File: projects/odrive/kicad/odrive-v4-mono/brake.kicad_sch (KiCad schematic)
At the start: 29 parts, among them J13 BRAKE_EXT, Q50 NVMFS5C628NL/BSC027N10NS5, Q51 NVMFS5C628NL/BSC027N10NS5, U50 UCC27517A, U51 INA181A2, U52 TLV7031, U53 74LVC1G74, U54 74LVC1G32, U55 74LVC1G08

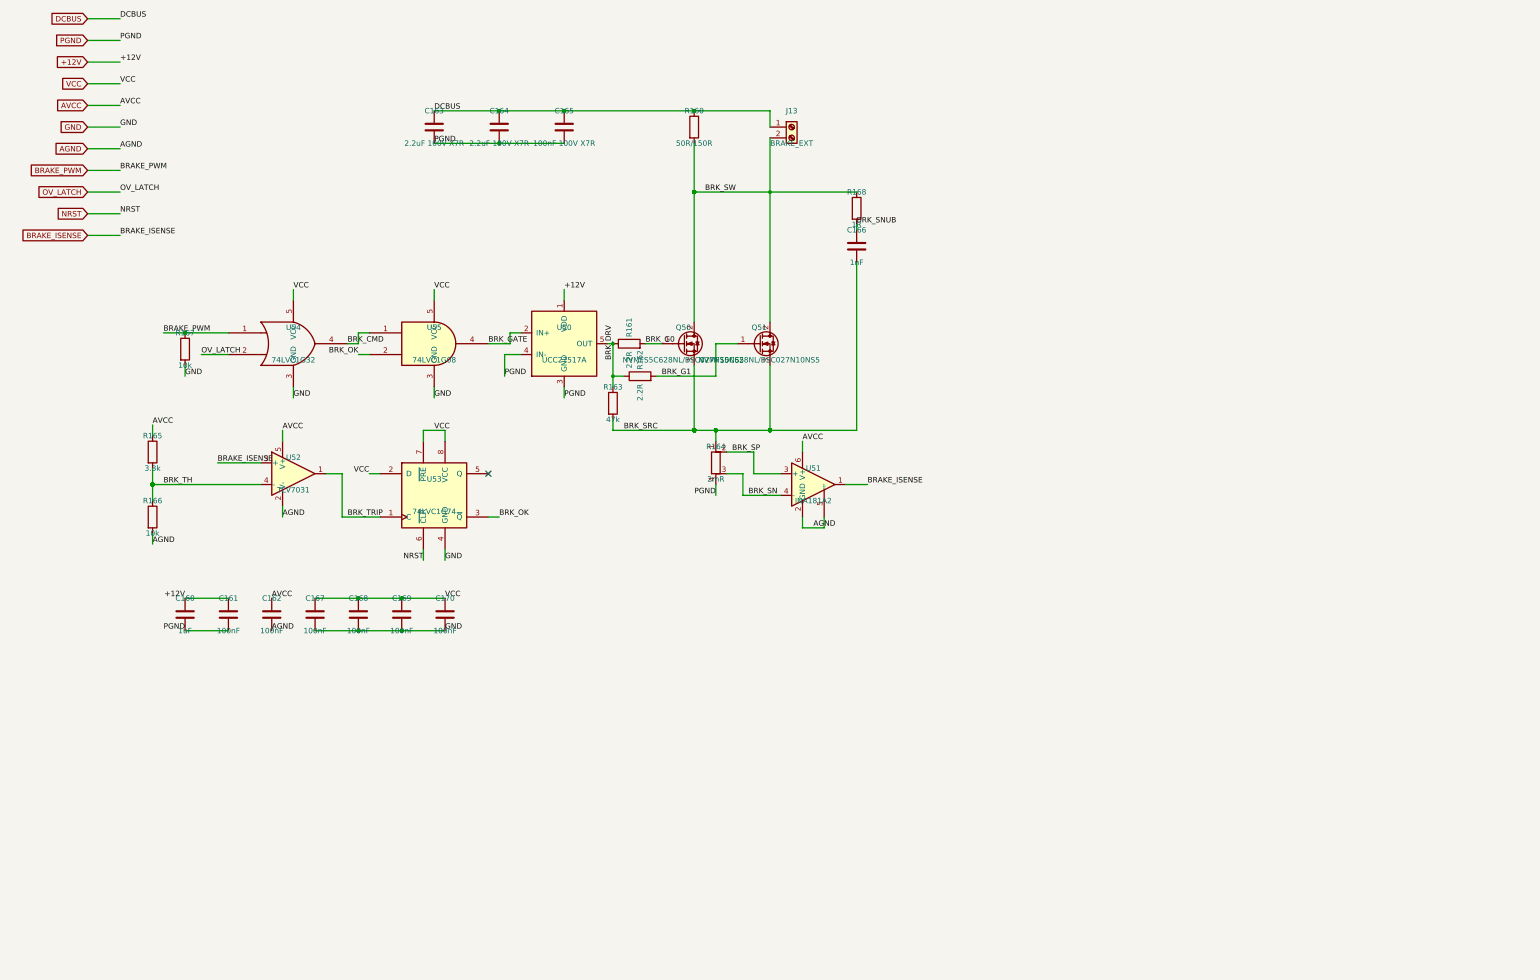
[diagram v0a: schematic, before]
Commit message: Checkpoint ODrive 56 V recovery and modular handoff
Preserve corrected schematics, local libraries, partial PCB routing, firmware diagnostics, analysis tools and the independent modular-study handoff. The board remains incomplete with 381 unconnected items and 415 DRC warnings.

Validation: 52 host tests, ARM component compilation, schematic/PCB parity, native copper preservation, DRC, STEP export, Python lint, shellcheck and nix fmt. Known Konnect-generated schematic whitespace is retained. No fabrication or hardware validation is claimed.
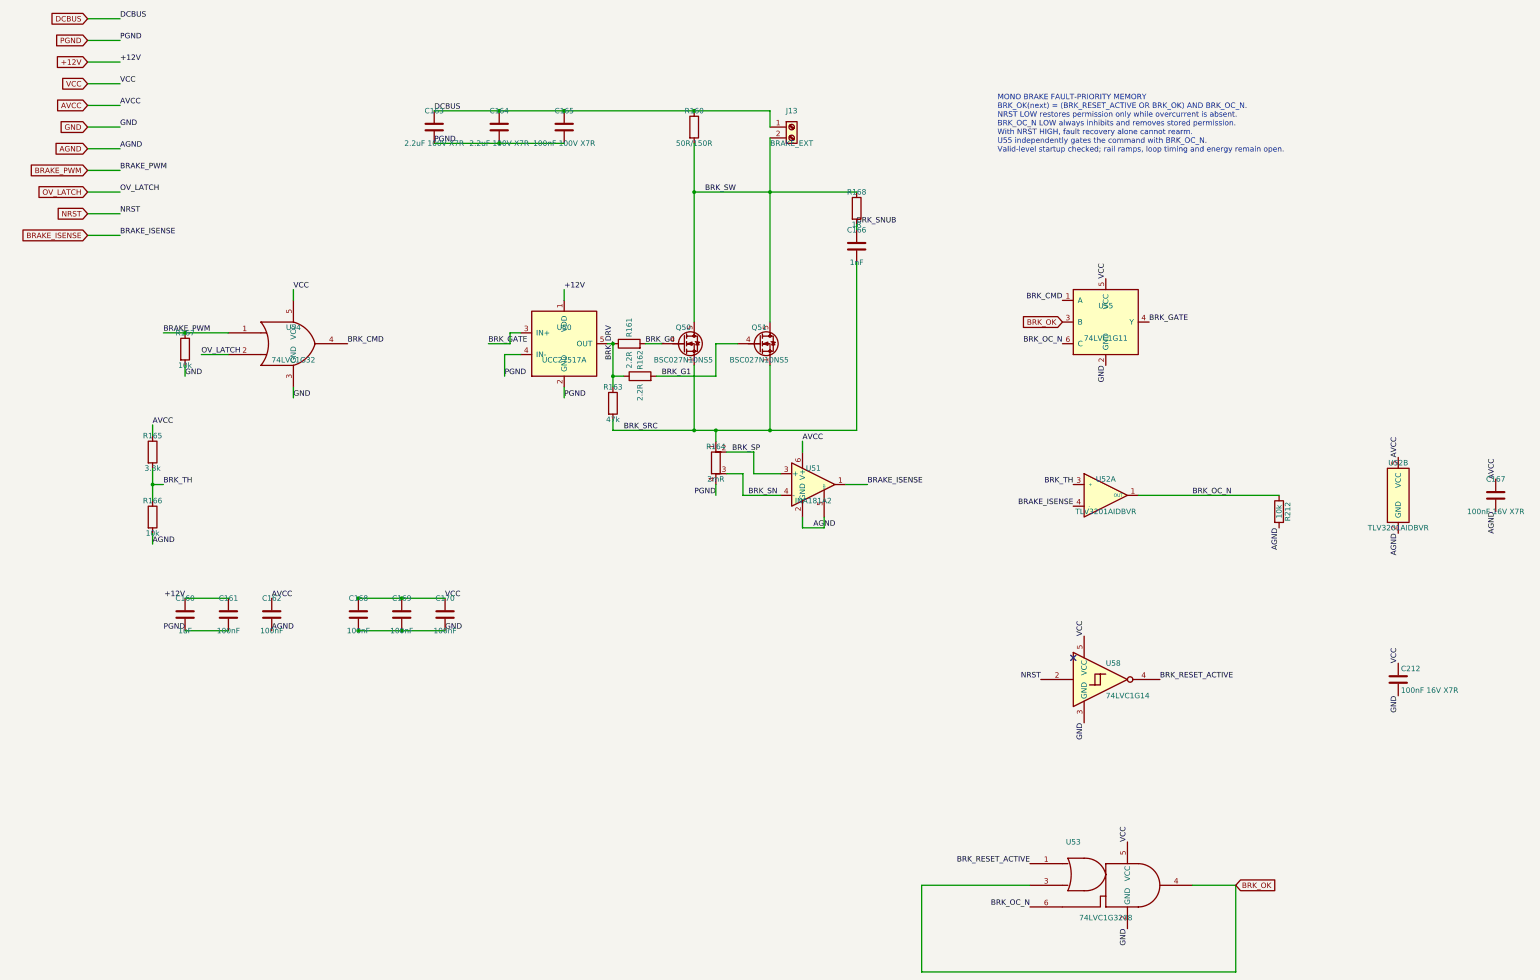
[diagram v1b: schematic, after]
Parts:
- added C212: 100nF 16V X7R, Capacitor_SMD:C_0603_1608Metric, symbol Device:C
- added R212: 10k, Resistor_SMD:R_0603_1608Metric, symbol Device:R
- added unit 2 of U52
- added U58: 74LVC1G14, Package_TO_SOT_SMD:SOT-23-5, symbol 74xGxx:74LVC1G14
- C167: value 100nF -> 100nF 16V X7R; Tolerance (none) -> 10%
- Q50, Q51: value NVMFS5C628NL/BSC027N10NS5 -> BSC027N10NS5; footprint Package_SO:PowerPAK_SO-8_Single -> odrive-mono:Infineon_PG-TSON-8-3; symbol Transistor_FET:Q_NMOS_GDS -> Transistor_FET:Q_NMOS_SSSGD_AvalancheRated; Design_note (none) -> 100V selection; verify losses, SOA, cooling and mask apertu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; MPN (none) -> BSC027N10NS5ATMA1; MPN_56V (none) -> BSC027N10NS5ATMA1; Manufacturer (none) -> Infineon
- U50: symbol /home/aldo/Dev/aldoborrero/cad/.claude/worktrees/odrive/projects/odrive/kicad/odrive-v4/odrive-v4-symbols:UCC27517A -> odrive-mono:UCC27517ADBV; MPN (none) -> UCC27517ADBVR; Manufacturer (none) -> Texas Instruments
- U52: value TLV7031 -> TLV3201AIDBVR; symbol Comparator:TLV7031DBV -> odrive-mono:TLV3201AIDBVR; MPN (none) -> TLV3201AIDBVR; Manufacturer (none) -> Texas Instruments
- U53: value 74LVC1G74 -> 74LVC1G3208; footprint Package_SO:TSSOP-8_3x3mm_P0.65mm -> Package_TO_SOT_SMD:SOT-23-6; symbol 74xGxx:74AUP1G74 -> 74xGxx:74LVC1G3208; MPN (none) -> SN74LVC1G3208DBVR; Manufacturer (none) -> Texas Instruments
- U55: value 74LVC1G08 -> 74LVC1G11; footprint Package_TO_SOT_SMD:SOT-23-5 -> Package_TO_SOT_SMD:SOT-23-6; symbol 74xGxx:74LVC1G08 -> odrive-mono:74LVC1G11DBV; MPN (none) -> SN74LVC1G11DBVR; Manufacturer (none) -> Texas Instruments
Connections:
- net AGND: now also C167.2, R212.2, U52.2 (GND); no longer U52.2 (V-)
- net AVCC: now also C167.1, U52.5 (VCC); no longer U52.5 (V+)
- net BRAKE_ISENSE: now also U52.4 (-); no longer U52.3 (+)
- net BRK_G0: now also Q50.4 (G); no longer Q50.1 (G)
- net BRK_G1: now also Q51.4 (G); no longer Q51.1 (G)
- net BRK_GATE: now also U50.3 (IN+); no longer U50.2 (IN+)
- net BRK_OK: now also U53.4, U55.3 (B); no longer U55.2
- net BRK_SRC: now also Q50.1 (S), Q50.2 (S), Q51.1 (S), Q51.2 (S)
- net BRK_SW: now also Q50.5 (D), Q51.5 (D); no longer Q50.2 (D), Q51.2 (D)
- net BRK_TH: now also U52.3 (+); no longer U52.4 (-)
- net GND: now also U53.2 (GND), U55.2 (GND), C212.2, U58.3 (GND); no longer C167.2, U53.4 (GND), U55.3 (GND)
- net NRST: now also U58.2; no longer U53.6 (~{CLR})
- net PGND: now also U50.2 (GND); no longer U50.3 (GND)
- net VCC: now also U53.5 (VCC), C212.1, U58.5 (VCC); no longer C167.1, U53.2 (D), U53.7 (~{PRE}), U53.8 (VCC)
- net BRK_TRIP renamed BRK_OC_N
- net BRK_OC_N: now also U53.6, U55.6 (C), R212.1; no longer U53.1 (C)
- new net BRK_RESET_ACTIVE: U53.1, U58.4
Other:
- note added: "MONO BRAKE FAULT-PRIORITY MEMORY BRK_OK(next) = (BRK_RESET_ACTIVE OR BRK_OK) AND BRK_OC_N. NRST LOW restores permission only while overcurrent is absent. BRK_OC_N LOW always inhibits and removes stored permission. With NRST HIGH, fault recovery alone cannot rearm. U55 independently gates the command with BRK_OC_N. Valid-level startup checked; rail ramps, loop timing and energy remain open."
- moved on the sheet: C167
